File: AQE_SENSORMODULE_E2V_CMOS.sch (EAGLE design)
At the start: 14 parts, among them IC1 TINY24/44/84-SSU, J1 440055-4, J2 AVR_SPI_PRG_6NS

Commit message: initial layout
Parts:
- renumbered U$1 to XT1, U$2 to U1
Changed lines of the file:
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@@
 <part name="R1" library="SparkFun" deviceset="RESISTOR" device="0805-RES" value="10 kOhm"/>
 <part name="P+2" library="SparkFun" deviceset="VCC" device=""/>
-<part name="U$1" library="wicked-device" deviceset="ABLS" device=""/>
+<part name="XT1" library="wicked-device" deviceset="ABLS" device=""/>
 <part name="C1" library="SparkFun" deviceset="CAP" device="0603-CAP"/>
 <part name="C2" library="SparkFun" deviceset="CAP" device="0603-CAP"/>
 <part name="SUPPLY2" library="supply2" deviceset="GND" device=""/>
-<part name="U$2" library="wicked-device" deviceset="LD1117XX" device=""/>
+<part name="U1" library="wicked-device" deviceset="LD1117XX" device=""/>
 <part name="SUPPLY3" library="supply2" deviceset="GND" device=""/>
 <part name="P+3" library="SparkFun" deviceset="VCC" device=""/>
@@
 <instance part="R1" gate="G$1" x="254" y="229.87" rot="R90"/>
 <instance part="P+2" gate="1" x="254" y="240.03"/>
-<instance part="U$1" gate="G$1" x="353.06" y="210.82" rot="R90"/>
+<instance part="XT1" gate="G$1" x="353.06" y="210.82" rot="R90"/>
 <instance part="C1" gate="G$1" x="337.82" y="199.39"/>
 <instance part="C2" gate="G$1" x="345.44" y="199.39"/>
 <instance part="SUPPLY2" gate="GND" x="341.63" y="193.04"/>
-<instance part="U$2" gate="G$1" x="95.25" y="187.96"/>
+<instance part="U1" gate="G$1" x="95.25" y="187.96"/>
 <instance part="SUPPLY3" gate="GND" x="95.25" y="162.56"/>
 <instance part="P+3" gate="1" x="68.58" y="210.82"/>
@@
 </segment>
 <segment>
-<pinref part="U$2" gate="G$1" pin="VI"/>
+<pinref part="U1" gate="G$1" pin="VI"/>
 <wire x1="82.55" y1="187.96" x2="68.58" y2="187.96" width="0.1524" layer="91"/>
 <pinref part="P+3" gate="1" pin="VCC"/>
@@
 </segment>
 <segment>
-<pinref part="U$2" gate="G$1" pin="GND"/>
+<pinref part="U1" gate="G$1" pin="GND"/>
 <wire x1="95.25" y1="177.8" x2="95.25" y2="167.64" width="0.1524" layer="91"/>
 <pinref part="SUPPLY3" gate="GND" pin="GND"/>
@@
 <net name="XTAL1" class="0">
 <segment>
-<pinref part="U$1" gate="G$1" pin="P$2"/>
+<pinref part="XT1" gate="G$1" pin="P$2"/>
 <wire x1="332.74" y1="215.9" x2="345.44" y2="215.9" width="0.1524" layer="91"/>
 <wire x1="345.44" y1="215.9" x2="353.06" y2="215.9" width="0.1524" layer="91"/>
@@
 <net name="XTAL2" class="0">
 <segment>
-<pinref part="U$1" gate="G$1" pin="P$1"/>
+<pinref part="XT1" gate="G$1" pin="P$1"/>
 <wire x1="332.74" y1="205.74" x2="337.82" y2="205.74" width="0.1524" layer="91"/>
 <pinref part="C1" gate="G$1" pin="1"/>
@@
 <net name="1.8V" class="0">
 <segment>
-<pinref part="U$2" gate="G$1" pin="VO"/>
+<pinref part="U1" gate="G$1" pin="VO"/>
 <wire x1="107.95" y1="187.96" x2="123.19" y2="187.96" width="0.1524" layer="91"/>
 <pinref part="U$3" gate="G$1" pin="1.8V"/>

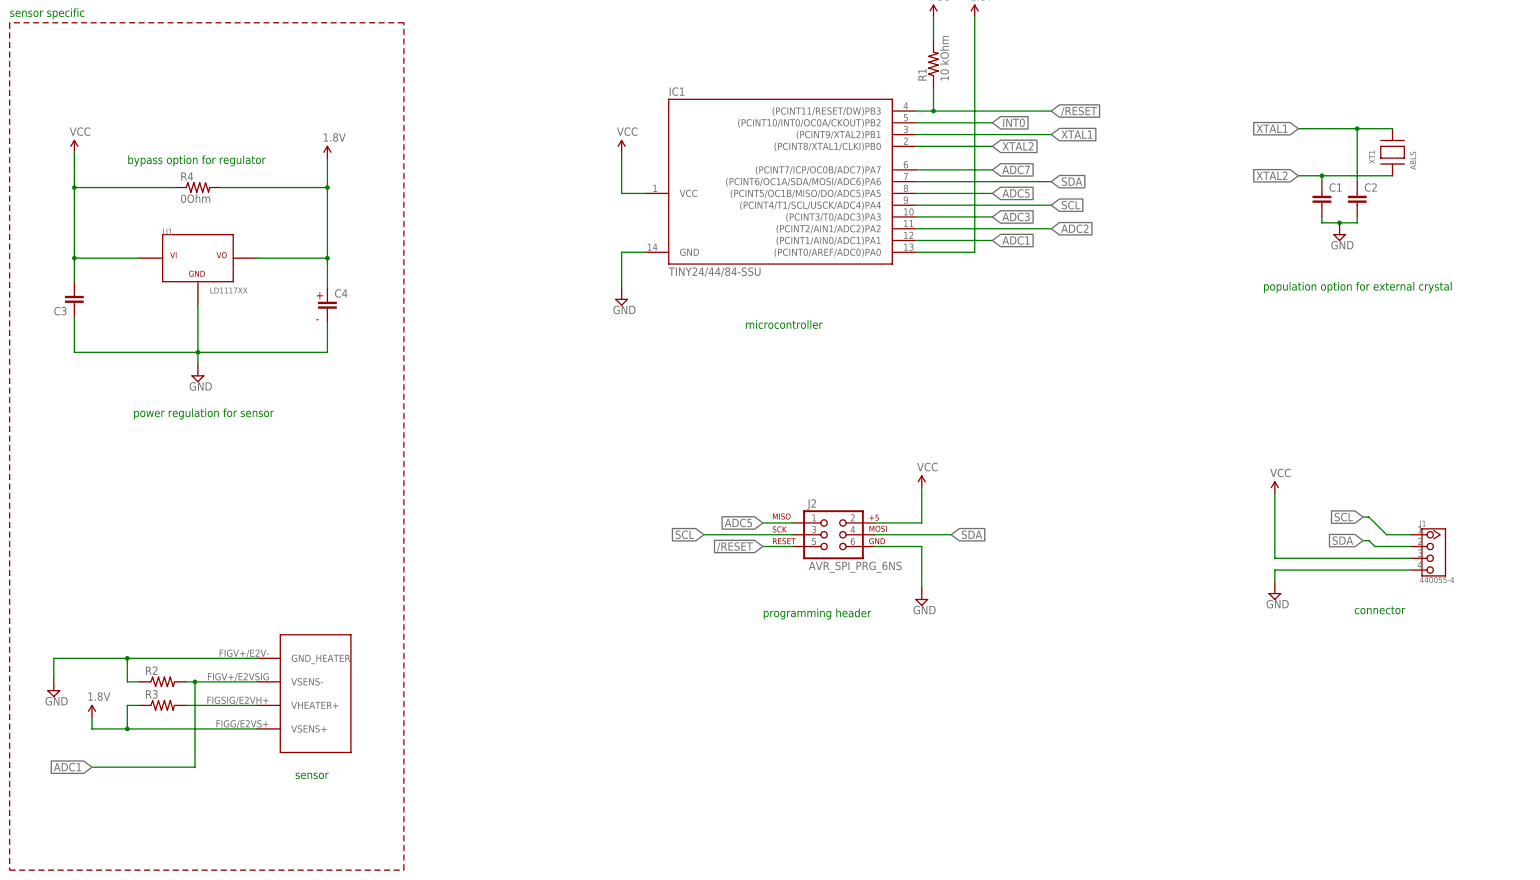
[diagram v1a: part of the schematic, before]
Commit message: aded MAC chip, switched to lm317 adjustable regulator, and re-routed the board by hand
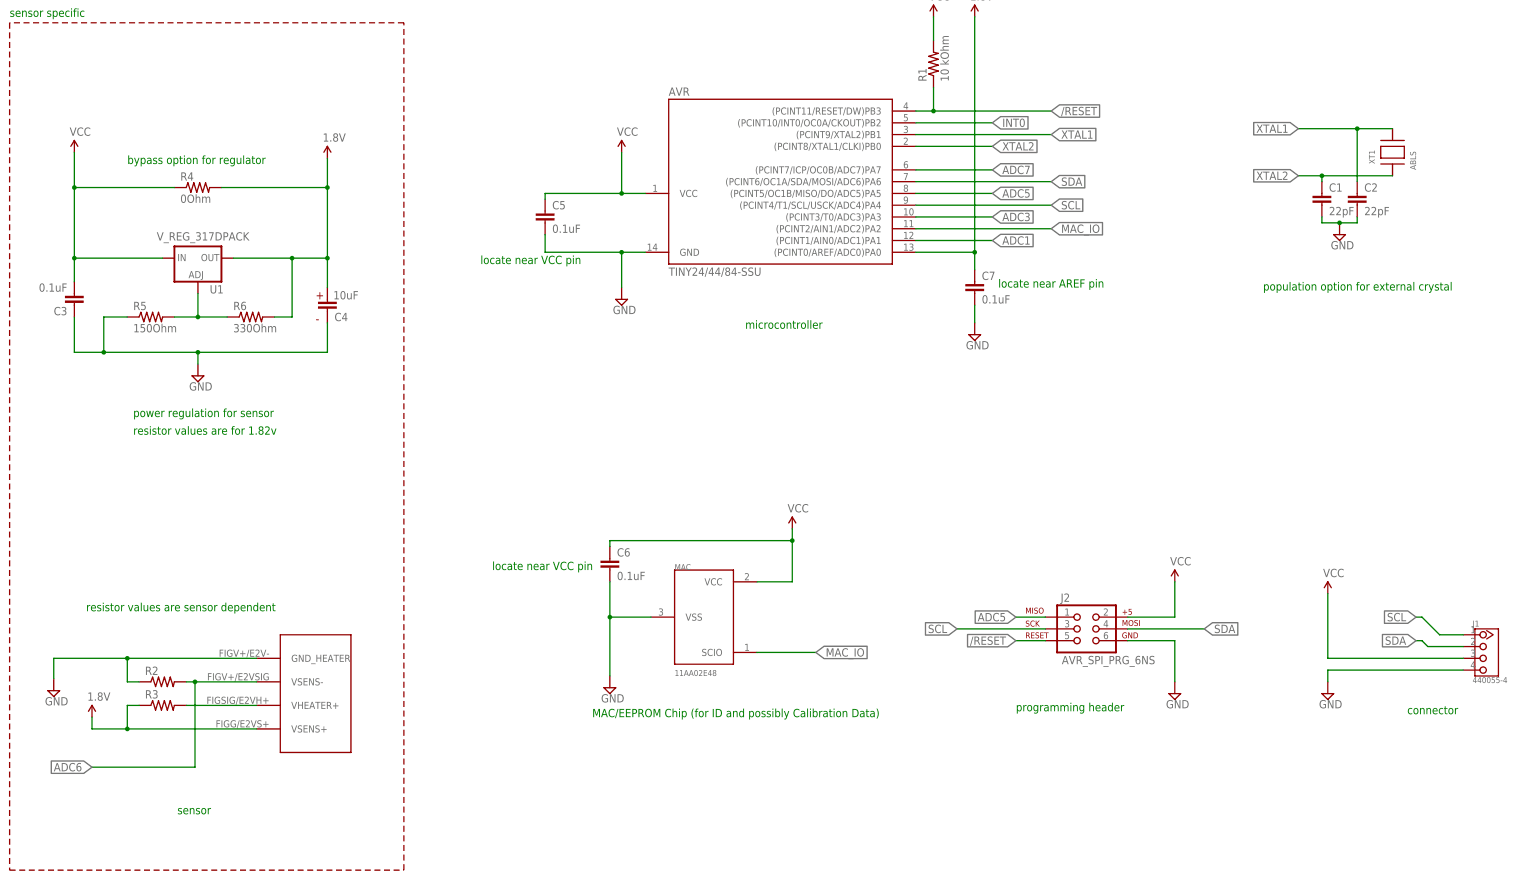
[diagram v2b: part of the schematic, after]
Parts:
- added C5, C6, C7: 0.1uF, SparkFun:CAP0603-CAP
- added MAC: 11AA02E48, nanode:11AA02E48
- added R5: 150Ohm, SparkFun:RESISTOR0805-RES
- added R6: 330Ohm, SparkFun:RESISTOR0805-RES
- C1, C2: value (none) -> 22pF
- C3: value (none) -> 0.1uF
- C4: value EEE-1EA100WR -> 10uF
- U1: value LD1117XX -> V_REG_317DPACK; device wicked-device:LD1117XX -> SparkFun:V_REG_317DPACK
- renumbered IC1 to AVR
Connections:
- removed net ADC2: AVR.(PCINT2/AIN1/ADC2)PA2
- new net ADC6: R2.2, U$4.VSENS-
- new net MAC_IO: AVR.(PCINT2/AIN1/ADC2)PA2, MAC.SCIO
- new net N$1: R5.2, R6.1, U1.ADJ
- net 1.8V: now also C7.1, R6.2, U1.OUT; no longer U1.VO
- net ADC1: no longer R2.2, U$4.VSENS-
- net GND: now also C5.2, C6.2, C7.2, MAC.VSS, R5.1; no longer U1.GND
- net VCC: now also C5.1, C6.1, MAC.VCC, U1.IN; no longer U1.VI
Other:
- note added: "10uF"
- note added: "MAC/EEPROM Chip (for ID and possibly Calibration Data)"
- note added: "locate near AREF pin"
- note added: "locate near VCC pin"
- note added: "resistor values are for 1.82v"
- note added: "resistor values are sensor dependent"
- moved on the sheet: J1, J2

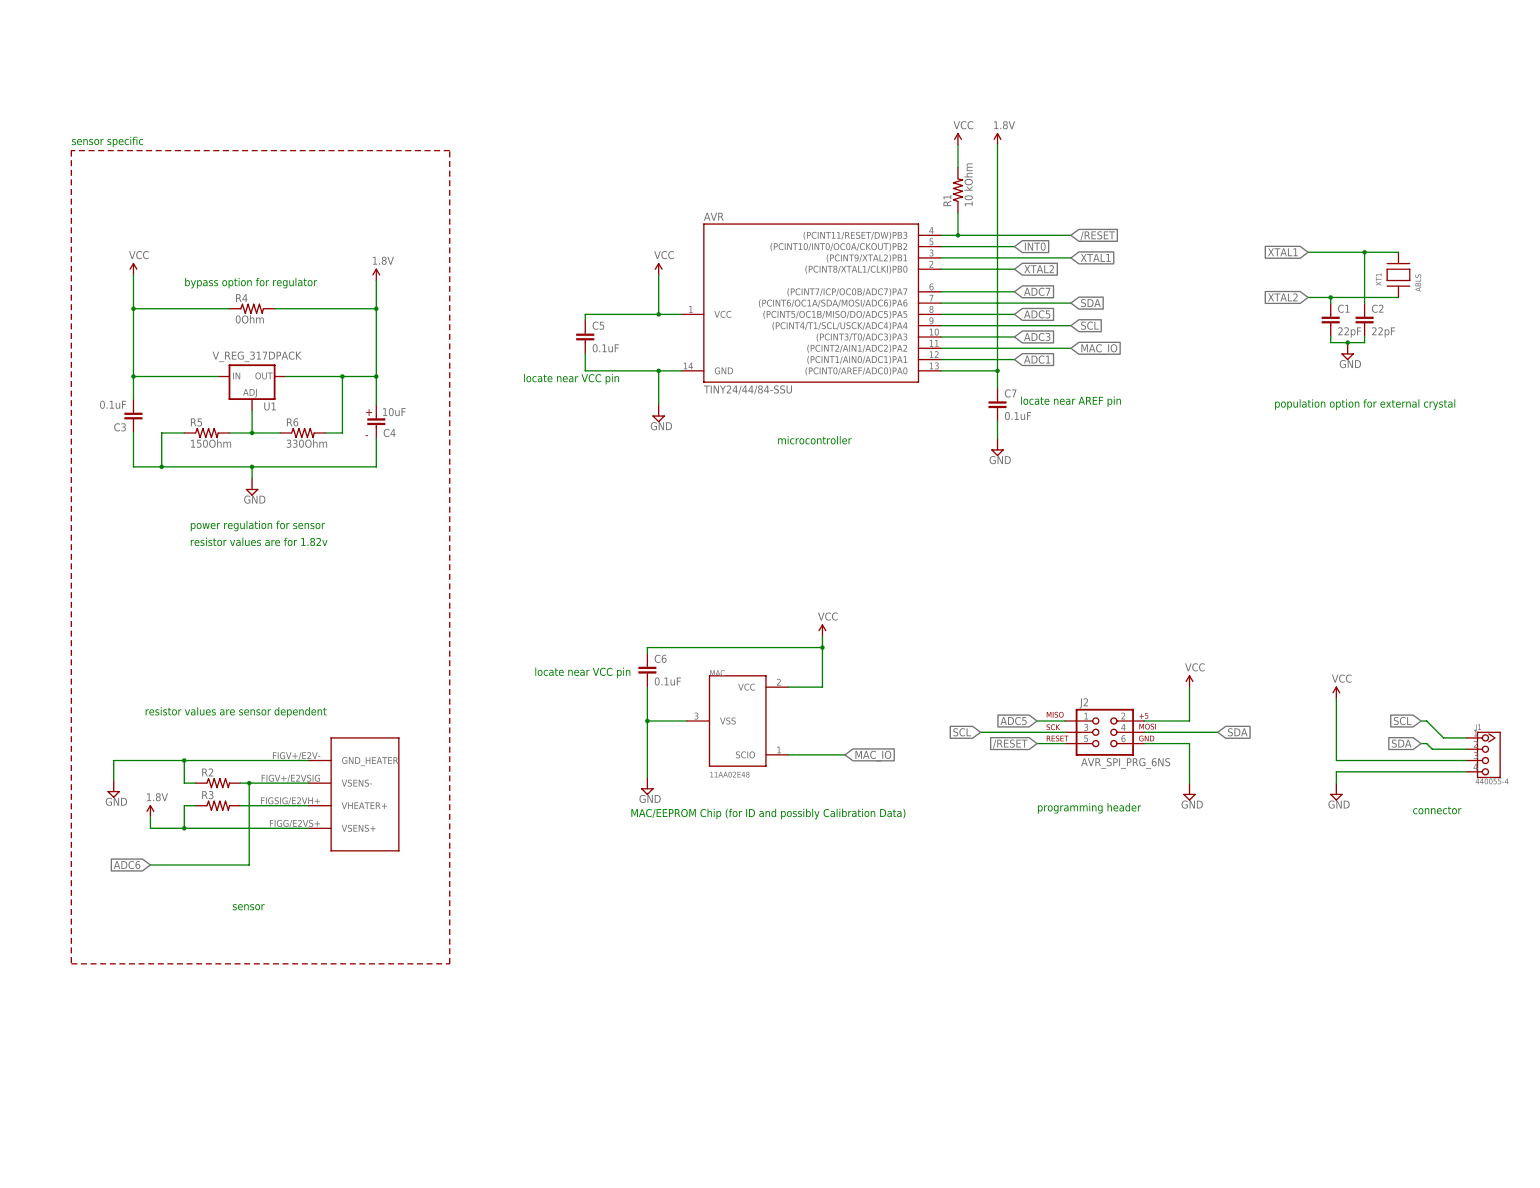
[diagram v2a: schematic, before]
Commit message: added second voltage regulator circuit, modified sensor circuit to allow 'sliding-scale' ADC approach, added standoff holes
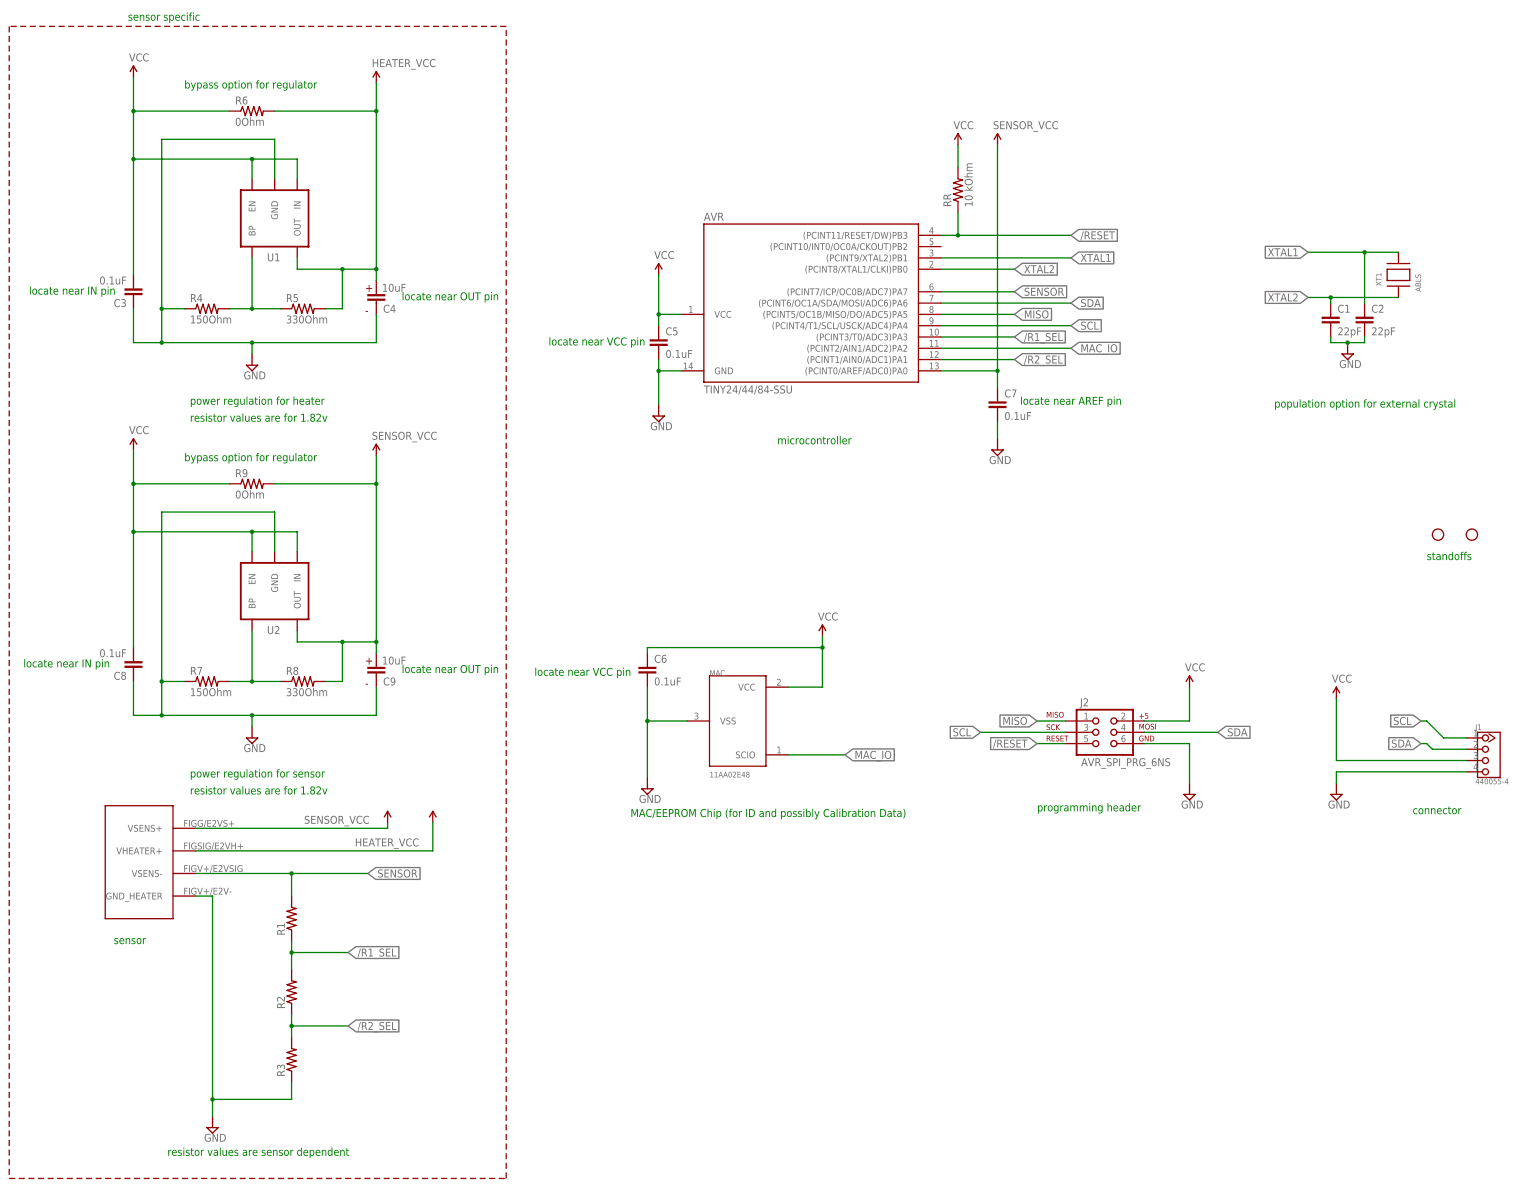
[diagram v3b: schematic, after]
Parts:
- added C8: 0.1uF, SparkFun:CAP0603-CAP
- added C9: 10uF, wicked-device:EEE-1EA100WR
- added JP1, JP2: STAND-OFF, SparkFun:STAND-OFF
- added R7: 150Ohm, SparkFun:RESISTOR0805-RES
- added R8: 330Ohm, SparkFun:RESISTOR0805-RES
- added R9: 0Ohm, SparkFun:RESISTOR0805-RES
- added RR: 10 kOhm, SparkFun:RESISTOR0805-RES
- added U2: V_REG_LDOSMD, SparkFun:V_REG_LDOSMD
- R1: value 10 kOhm -> (none)
- R4: value 0Ohm -> 150Ohm
- R5: value 150Ohm -> 330Ohm
- R6: value 330Ohm -> 0Ohm
- U1: value V_REG_317DPACK -> V_REG_LDOSMD; device SparkFun:V_REG_317DPACK -> SparkFun:V_REG_LDOSMD
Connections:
- net ADC5 renamed MISO
- removed net 1.8V: AVR.(PCINT0/AREF/ADC0)PA0, C4.1, C7.1, R3.1, R4.2, R6.2, U$4.VSENS+, U1.OUT
- removed net ADC1: AVR.(PCINT1/AIN0/ADC1)PA1
- removed net ADC3: AVR.(PCINT3/T0/ADC3)PA3
- removed net ADC6: R2.2, U$4.VSENS-
- removed net ADC7: AVR.(PCINT7/ICP/OC0B/ADC7)PA7
- removed net INT0: AVR.(PCINT10/INT0/OC0A/CKOUT)PB2
- removed net N$3: R3.2, U$4.VHEATER+
- new net /R1_SEL: AVR.(PCINT3/T0/ADC3)PA3, R1.1, R2.2
- new net /R2_SEL: AVR.(PCINT1/AIN0/ADC1)PA1, R2.1, R3.2
- new net HEATER_VCC: C4.1, R5.2, R6.2, U$4.VHEATER+, U1.OUT
- new net N$2: R7.2, R8.1, U2.BP
- new net SENSOR: AVR.(PCINT7/ICP/OC0B/ADC7)PA7, R1.2, U$4.VSENS-
- new net SENSOR_VCC: AVR.(PCINT0/AREF/ADC0)PA0, C7.1, C9.1, R8.2, R9.2, U$4.VSENS+, U2.OUT
- net /RESET: now also RR.1; no longer R1.1
- net GND: now also C8.1, C9.2, R3.1, R4.1, R7.1, U1.GND, U2.GND; no longer R2.1, R5.1
- net N$1: now also R4.2, R5.1, U1.BP; no longer R5.2, R6.1, U1.ADJ
- net VCC: now also C8.2, R6.1, R9.1, RR.2, U1.EN, U2.EN, U2.IN; no longer R1.2, R4.1
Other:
- note added: "locate near IN pin"
- note added: "locate near OUT pin"
- note added: "power regulation for heater"
- note added: "standoffs"
- moved on the sheet: C3, C4, C5, R1, R2, R3, R4, R5, R6
